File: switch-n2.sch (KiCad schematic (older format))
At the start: 43 parts, among them J1 61000821121, Q1 ZXMP10A13F, Q2 NVMFS6H800NT1G, Q3 NVMFS6H800NT1G, Q4 NVMFS6H800NT1G, Q5 NVMFS6H800NT1G, U1 BQ76200

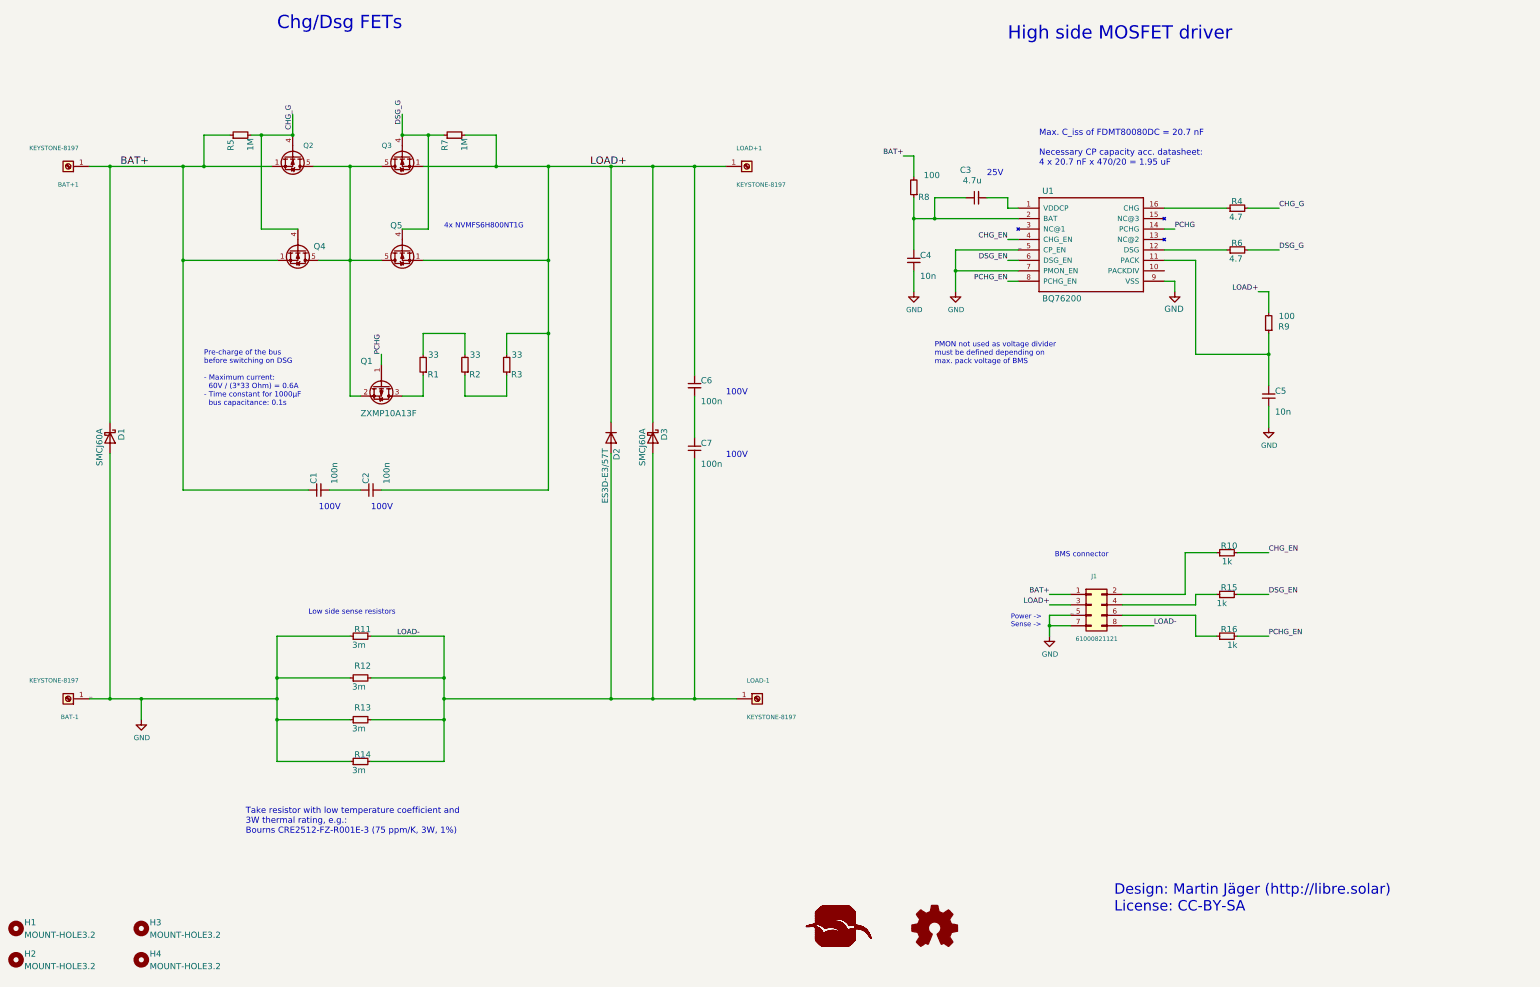
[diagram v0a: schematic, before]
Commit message: Fixed some comments on schematic
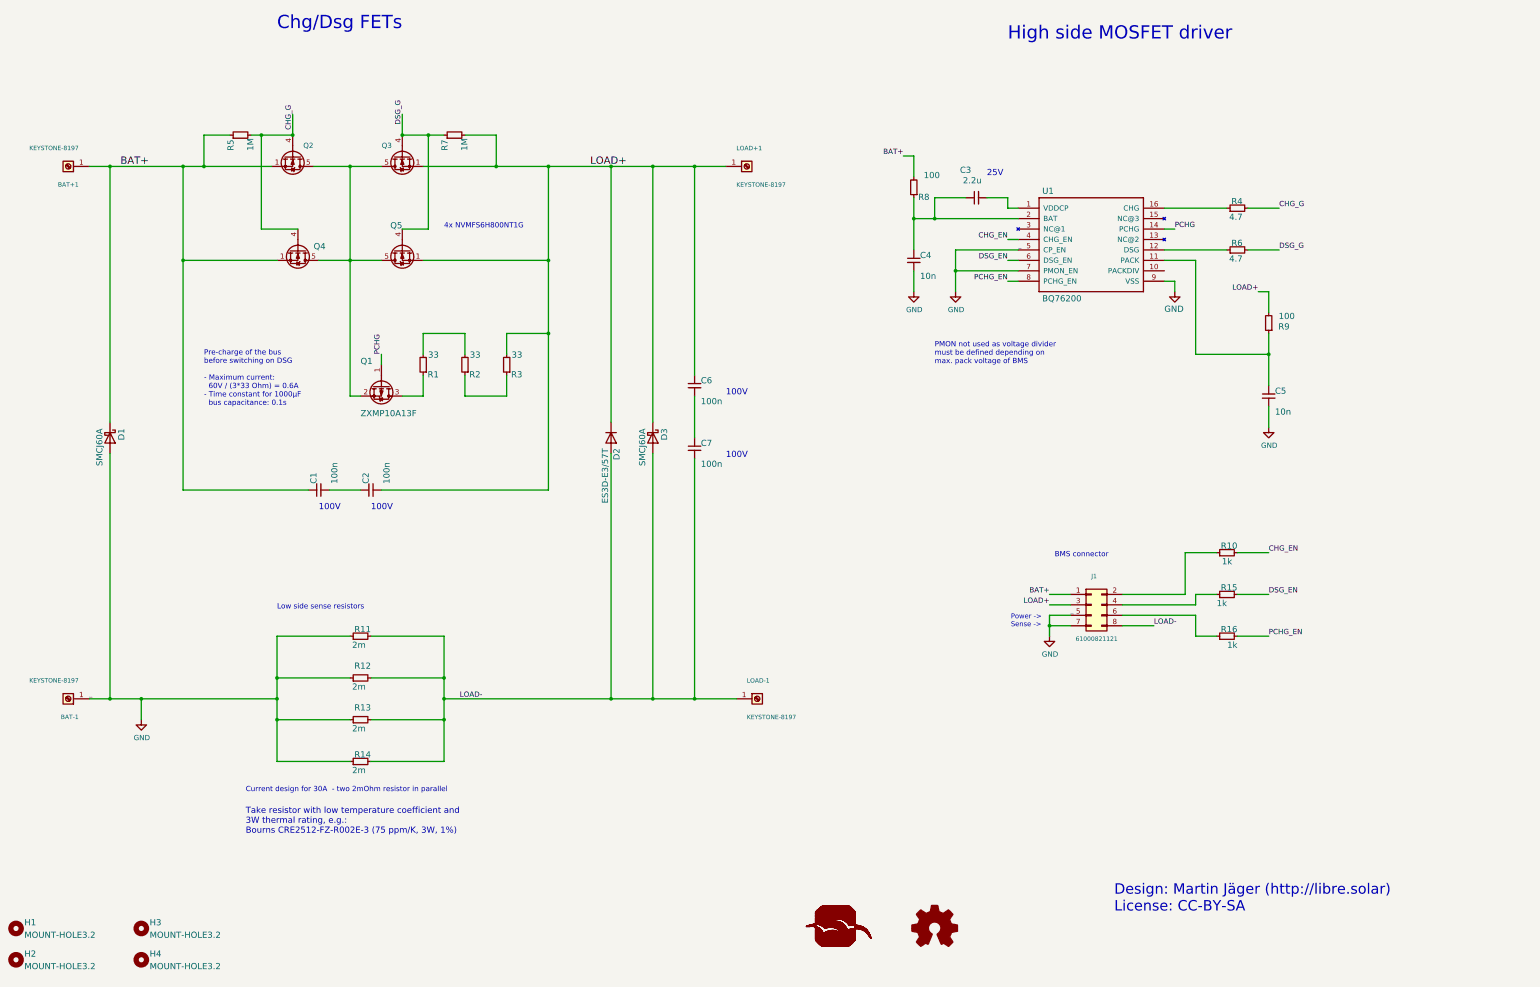
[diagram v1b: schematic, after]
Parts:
- C3: value 4.7u -> 2.2u
- R11, R12, R13, R14: value 3m -> 2m; OC_FARNELL unknown -> 2434011
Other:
- note added: "Current design for 30A - two 2mOhm resistor in parallel"
- note added: "Low side sense resistors\n"
- note added: "Take resistor with low temperature coefficient and \n3W thermal rating, e.g.:\nBourns CRE2512-FZ-R002E-3 (75 ppm/K, 3W, 1%)"
- note removed: "Low side sense resistors"
- note removed: "Max. C_iss of FDMT80080DC = 20.7 nF\n\nNecessary CP capacity acc. datasheet:\n4 x 20.7 nF x 470/20 = 1.95 uF"
- note removed: "Take resistor with low temperature coefficient and \n3W thermal rating, e.g.:\nBourns CRE2512-FZ-R001E-3 (75 ppm/K, 3W, 1%)"
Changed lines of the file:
@@
 P 11000 2500
 F 0 "C3" V 11300 2550 59  0000 L BNN
-F 1 "4.7u" V 11200 2450 59  0000 L BNN
+F 1 "2.2u" V 11200 2450 59  0000 L BNN
 F 2 "Capacitor_SMD:C_0805_2012Metric" H 11000 2500 50  0001 C CNN
 F 3 "" H 11000 2500 50  0001 C CNN
@@
 P 5100 6700
 F 0 "R11" V 5200 6600 59  0000 L BNN
-F 1 "3m" V 5050 6650 59  0000 L BNN
+F 1 "2m" V 5050 6650 59  0000 L BNN
 F 2 "Resistor_SMD:R_2512_6332Metric" H 5100 6700 50  0001 C CNN
-F 3 "" H 5100 6700 50  0001 C CNN
-F 4 "unknown" H 5100 6700 59  0001 L BNN "OC_FARNELL"
+F 3 "www.farnell.com/datasheets/2059712.pdf" H 5100 6700 50  0001 C CNN
+F 4 "2434011" H 5100 6700 59  0001 L BNN "OC_FARNELL"
 	1    5100 6700
 	0    -1   -1   0
@@
 P 5100 7100
 F 0 "R12" V 5250 7000 59  0000 L BNN
-F 1 "3m" V 5050 7050 59  0000 L BNN
+F 1 "2m" V 5050 7050 59  0000 L BNN
 F 2 "Resistor_SMD:R_2512_6332Metric" H 5100 7100 50  0001 C CNN
 F 3 "" H 5100 7100 50  0001 C CNN
-F 4 "unknown" H 5100 7100 59  0001 L BNN "OC_FARNELL"
+F 4 "2434011 " H 5100 7100 59  0001 L BNN "OC_FARNELL"
 	1    5100 7100
 	0    -1   -1   0
@@
 P 5100 7500
 F 0 "R13" V 5250 7400 59  0000 L BNN
-F 1 "3m" V 5050 7450 59  0000 L BNN
+F 1 "2m" V 5050 7450 59  0000 L BNN
 F 2 "Resistor_SMD:R_2512_6332Metric" H 5100 7500 50  0001 C CNN
 F 3 "" H 5100 7500 50  0001 C CNN
-F 4 "unknown" H 5100 7500 59  0001 L BNN "OC_FARNELL"
+F 4 "2434011 " H 5100 7500 59  0001 L BNN "OC_FARNELL"
 	1    5100 7500
 	0    -1   -1   0
@@
 P 5100 7900
 F 0 "R14" V 5200 7800 59  0000 L BNN
-F 1 "3m" V 5050 7850 59  0000 L BNN
+F 1 "2m" V 5050 7850 59  0000 L BNN
 F 2 "Resistor_SMD:R_2512_6332Metric" H 5100 7900 50  0001 C CNN
 F 3 "" H 5100 7900 50  0001 C CNN
-F 4 "unknown" H 5100 7900 59  0001 L BNN "OC_FARNELL"
+F 4 "2434011 " H 5100 7900 59  0001 L BNN "OC_FARNELL"
 	1    5100 7900
 	0    -1   -1   0
@@
 Text Notes 12320 9350 0    100  ~ 0
 Design: Martin Jäger (http://libre.solar)\nLicense: CC-BY-SA
-Text Notes 11600 2200 0    59   ~ 0
-Max. C_iss of FDMT80080DC = 20.7 nF\n\nNecessary CP capacity acc. datasheet:\n4 x 20.7 nF x 470/20 = 1.95 uF
 Text Notes 5900 2800 0    50   ~ 0
 4x NVMFS6H800NT1G
 Text Notes 4000 8600 0    59   ~ 0
-Take resistor with low temperature coefficient and \n3W thermal rating, e.g.:\nBourns CRE2512-FZ-R001E-3 (75 ppm/K, 3W, 1%)
-Text Notes 4600 6500 0    50   ~ 0
-Low side sense resistors
+Take resistor with low temperature coefficient and \n3W thermal rating, e.g.:\nBourns CRE2512-FZ-R002E-3 (75 ppm/K, 3W, 1%)
+Text Notes 4300 6450 0    50   ~ 0
+Low side sense resistors\n
 Text Notes 11750 5950 0    50   ~ 0
 BMS connector
@@
 Wire Wire Line
 	4300 6700 5000 6700
-Text Label 5450 6700 0    50   ~ 0
+Text Label 6050 7300 0    50   ~ 0
 LOAD-
 Wire Wire Line
@@
 	0    1    1    0
 $EndComp
+Text Notes 4000 8200 0    50   ~ 0
+Current design for 30A  - two 2mOhm resistor in parallel
 $EndSCHEMATC

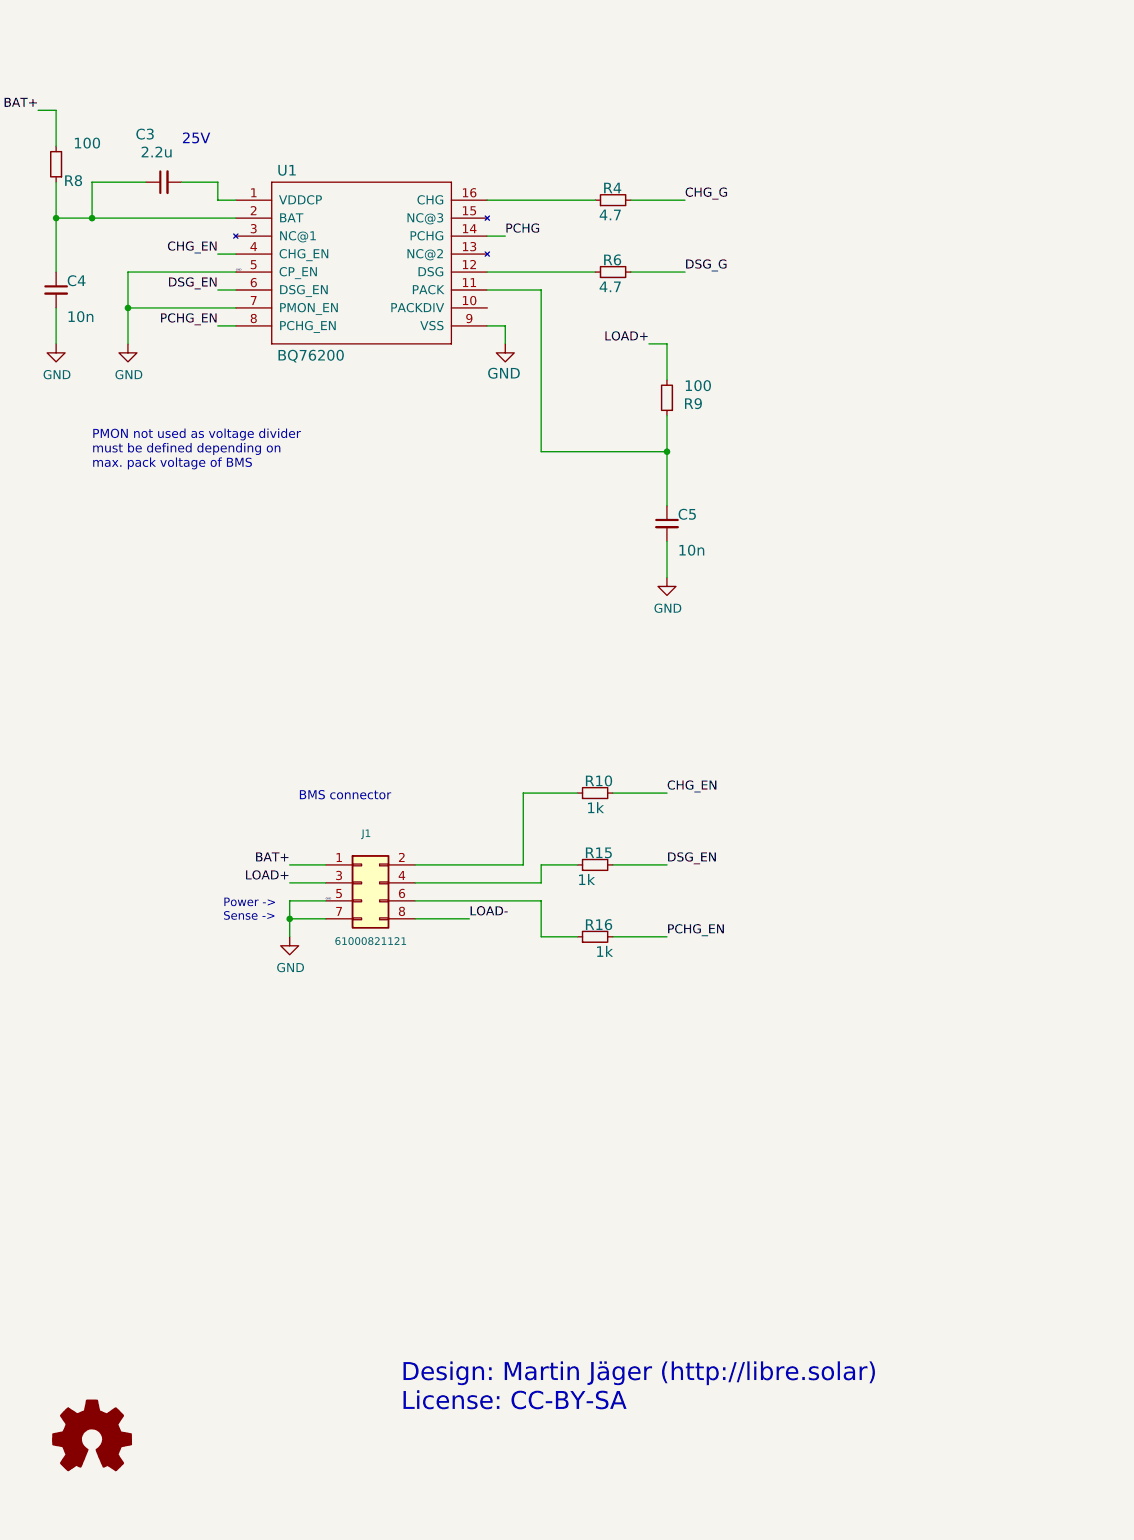
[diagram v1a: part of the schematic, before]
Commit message: Clean up schematics and add pdf version
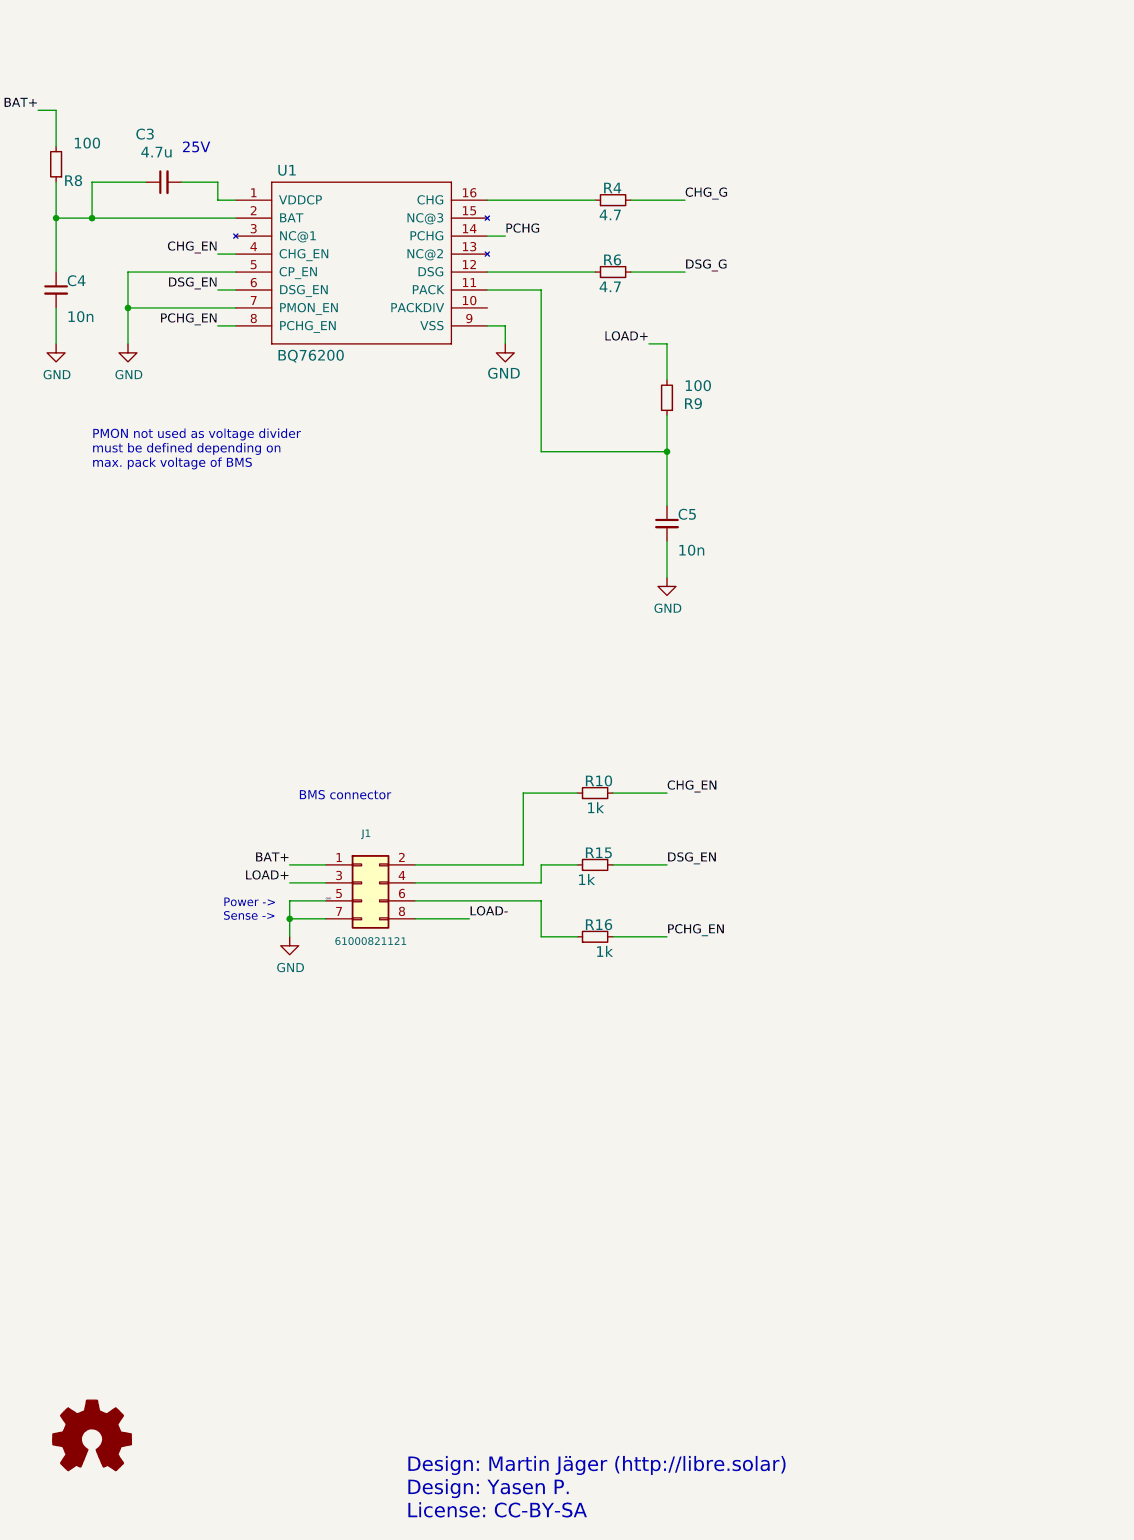
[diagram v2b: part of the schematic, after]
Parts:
- C3: value 2.2u -> 4.7u
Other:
- note added: "Design: Martin Jäger (http://libre.solar)\nDesign: Yasen P.\nLicense: CC-BY-SA"
- note removed: "Design: Martin Jäger (http://libre.solar)\nLicense: CC-BY-SA"
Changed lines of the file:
@@
 	11400 3200 10800 3200
 Connection ~ 10800 3200
-Text Label 11400 3000 0    10   ~ 0
-GND
 Wire Wire Line
 	12800 2600 13400 2600
@@
 P 11000 2500
 F 0 "C3" V 11300 2550 59  0000 L BNN
-F 1 "2.2u" V 11200 2450 59  0000 L BNN
+F 1 "4.7u" V 11200 2450 59  0000 L BNN
 F 2 "Capacitor_SMD:C_0805_2012Metric" H 11000 2500 50  0001 C CNN
 F 3 "" H 11000 2500 50  0001 C CNN
@@
 Text Notes 11300 1000 0    127  ~ 0
 High side MOSFET driver
-Text Notes 12320 9350 0    100  ~ 0
-Design: Martin Jäger (http://libre.solar)\nLicense: CC-BY-SA
+Text Notes 12350 9950 0    80   ~ 0
+Design: Martin Jäger (http://libre.solar)\nDesign: Yasen P.\nLicense: CC-BY-SA
 Text Notes 5900 2800 0    50   ~ 0
 4x NVMFS6H800NT1G
@@
 Text Notes 5200 5500 0    59   ~ 0
 100V
-Text Notes 4700 5500 0    59   ~ 0
-100V
-Text Notes 11100 2300 0    59   ~ 0
+Text Notes 11100 2350 0    59   ~ 0
 25V
 Wire Wire Line
@@
 Text Notes 4000 8200 0    50   ~ 0
 Current design for 30A  - two 2mOhm resistor in parallel
+Text Notes 4700 5500 0    59   ~ 0
+100V
 $EndSCHEMATC
